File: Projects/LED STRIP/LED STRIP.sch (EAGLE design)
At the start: 70 parts, among them U1 PCA9635, U2 PCA9635, U3 PCA9635

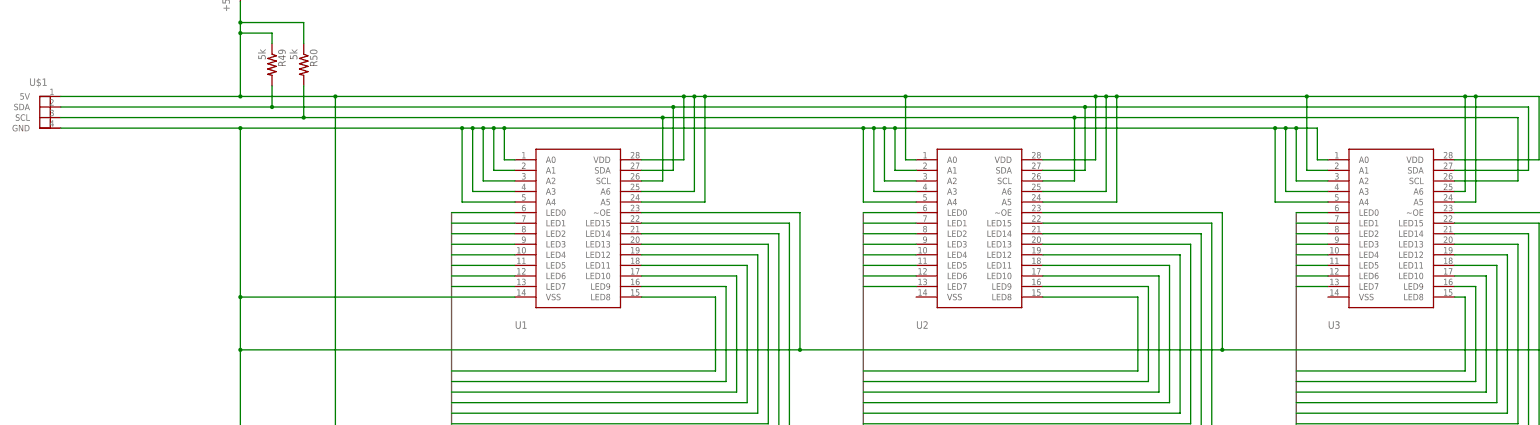
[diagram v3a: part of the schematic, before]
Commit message: design is done. ERC, DRC, air wires all pass. next up: integrate bluetooth components
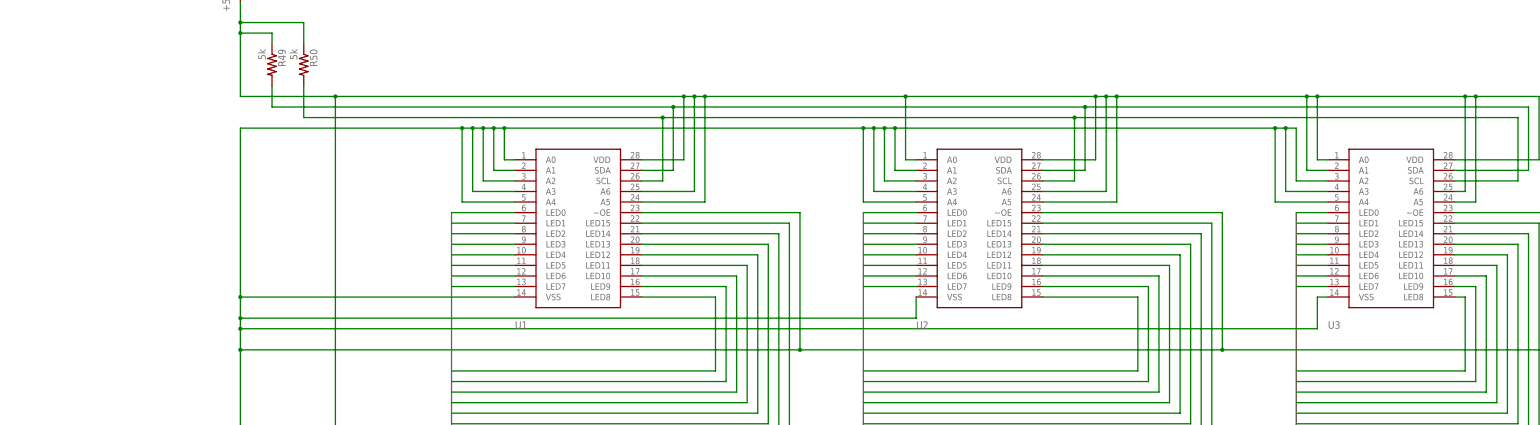
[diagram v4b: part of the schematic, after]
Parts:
- removed U$1: I2C_CONN, lightsuits:I2C_CONN
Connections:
- removed net N$51: R49.2, U$1.SDA, U1.SDA, U2.SDA, U3.SDA
- removed net N$52: R50.2, U$1.SCL, U1.SCL, U2.SCL, U3.SCL
- new net SCL: R50.2, U1.SCL, U2.SCL, U3.SCL
- new net SDA: R49.2, U1.SDA, U2.SDA, U3.SDA
- net +5V: now also U3.A0; no longer U$1.5V
- net GND: now also U2.VSS, U3.VSS; no longer U$1.GND, U3.A0
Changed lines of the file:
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@@
 <part name="P+1" library="supply1" deviceset="+5V" device=""/>
 <part name="GND1" library="supply1" deviceset="GND" device=""/>
-<part name="U$1" library="lightsuits" deviceset="I2C_CONN" device=""/>
 <part name="LED3" library="lightsuits" deviceset="LED_RGB" device=""/>
 <part name="LED4" library="lightsuits" deviceset="LED_RGB" device=""/>
@@
 <instance part="P+1" gate="1" x="-38.1" y="200.66"/>
 <instance part="GND1" gate="1" x="-38.1" y="5.08"/>
-<instance part="U$1" gate="G$1" x="-83.82" y="175.26"/>
 <instance part="LED3" gate="G$1" x="73.66" y="50.8"/>
 <instance part="LED4" gate="G$1" x="88.9" y="50.8"/>
@@
 <wire x1="-38.1" y1="7.62" x2="-38.1" y2="114.3" width="0.1524" layer="91"/>
 <pinref part="U1" gate="G$1" pin="VSS"/>
-<wire x1="-38.1" y1="114.3" x2="-38.1" y2="127" width="0.1524" layer="91"/>
+<wire x1="-38.1" y1="114.3" x2="-38.1" y2="119.38" width="0.1524" layer="91"/>
+<wire x1="-38.1" y1="119.38" x2="-38.1" y2="121.92" width="0.1524" layer="91"/>
+<wire x1="-38.1" y1="121.92" x2="-38.1" y2="127" width="0.1524" layer="91"/>
 <wire x1="-38.1" y1="127" x2="27.94" y2="127" width="0.1524" layer="91"/>
-<pinref part="U$1" gate="G$1" pin="GND"/>
-<wire x1="-81.28" y1="167.64" x2="-38.1" y2="167.64" width="0.1524" layer="91"/>
 <wire x1="-38.1" y1="167.64" x2="-38.1" y2="127" width="0.1524" layer="91"/>
 <junction x="-38.1" y="127"/>
@@
 <wire x1="116.84" y1="167.64" x2="119.38" y2="167.64" width="0.1524" layer="91"/>
 <wire x1="119.38" y1="167.64" x2="210.82" y2="167.64" width="0.1524" layer="91"/>
-<junction x="-38.1" y="167.64"/>
 <pinref part="U1" gate="G$1" pin="A0"/>
 <wire x1="210.82" y1="167.64" x2="213.36" y2="167.64" width="0.1524" layer="91"/>
 <wire x1="213.36" y1="167.64" x2="215.9" y2="167.64" width="0.1524" layer="91"/>
-<wire x1="215.9" y1="167.64" x2="220.98" y2="167.64" width="0.1524" layer="91"/>
 <wire x1="27.94" y1="160.02" x2="25.4" y2="160.02" width="0.1524" layer="91"/>
 <wire x1="25.4" y1="160.02" x2="25.4" y2="167.64" width="0.1524" layer="91"/>
@@
 <wire x1="119.38" y1="157.48" x2="119.38" y2="167.64" width="0.1524" layer="91"/>
 <junction x="119.38" y="167.64"/>
-<pinref part="U3" gate="G$1" pin="A0"/>
-<wire x1="223.52" y1="160.02" x2="220.98" y2="160.02" width="0.1524" layer="91"/>
-<wire x1="220.98" y1="160.02" x2="220.98" y2="167.64" width="0.1524" layer="91"/>
 <pinref part="U3" gate="G$1" pin="A2"/>
 <wire x1="223.52" y1="154.94" x2="215.9" y2="154.94" width="0.1524" layer="91"/>
 <wire x1="215.9" y1="154.94" x2="215.9" y2="167.64" width="0.1524" layer="91"/>
-<junction x="215.9" y="167.64"/>
 <pinref part="U2" gate="G$1" pin="A2"/>
 <wire x1="124.46" y1="154.94" x2="116.84" y2="154.94" width="0.1524" layer="91"/>
@@
 <wire x1="210.82" y1="149.86" x2="210.82" y2="167.64" width="0.1524" layer="91"/>
 <junction x="210.82" y="167.64"/>
+<pinref part="U2" gate="G$1" pin="VSS"/>
+<wire x1="124.46" y1="127" x2="124.46" y2="121.92" width="0.1524" layer="91"/>
+<wire x1="124.46" y1="121.92" x2="-38.1" y2="121.92" width="0.1524" layer="91"/>
+<junction x="-38.1" y="121.92"/>
+<pinref part="U3" gate="G$1" pin="VSS"/>
+<wire x1="223.52" y1="127" x2="220.98" y2="127" width="0.1524" layer="91"/>
+<wire x1="220.98" y1="127" x2="220.98" y2="119.38" width="0.1524" layer="91"/>
+<wire x1="220.98" y1="119.38" x2="-38.1" y2="119.38" width="0.1524" layer="91"/>
+<junction x="-38.1" y="119.38"/>
 </segment>
 </net>
@@
 <pinref part="P+1" gate="1" pin="+5V"/>
 <wire x1="-38.1" y1="198.12" x2="-38.1" y2="193.04" width="0.1524" layer="91"/>
-<pinref part="U$1" gate="G$1" pin="5V"/>
 <wire x1="-38.1" y1="193.04" x2="-38.1" y2="190.5" width="0.1524" layer="91"/>
 <wire x1="-38.1" y1="190.5" x2="-38.1" y2="175.26" width="0.1524" layer="91"/>
-<wire x1="-38.1" y1="175.26" x2="-81.28" y2="175.26" width="0.1524" layer="91"/>
 <wire x1="-38.1" y1="175.26" x2="-15.24" y2="175.26" width="0.1524" layer="91"/>
 <wire x1="-15.24" y1="175.26" x2="68.58" y2="175.26" width="0.1524" layer="91"/>
 <wire x1="68.58" y1="175.26" x2="68.58" y2="160.02" width="0.1524" layer="91"/>
-<junction x="-38.1" y="175.26"/>
 <pinref part="U1" gate="G$1" pin="VDD"/>
 <wire x1="68.58" y1="160.02" x2="58.42" y2="160.02" width="0.1524" layer="91"/>
@@
 <wire x1="170.18" y1="175.26" x2="172.72" y2="175.26" width="0.1524" layer="91"/>
 <wire x1="172.72" y1="175.26" x2="218.44" y2="175.26" width="0.1524" layer="91"/>
-<wire x1="218.44" y1="175.26" x2="256.54" y2="175.26" width="0.1524" layer="91"/>
+<wire x1="218.44" y1="175.26" x2="220.98" y2="175.26" width="0.1524" layer="91"/>
+<wire x1="220.98" y1="175.26" x2="256.54" y2="175.26" width="0.1524" layer="91"/>
 <wire x1="256.54" y1="175.26" x2="259.08" y2="175.26" width="0.1524" layer="91"/>
 <wire x1="259.08" y1="175.26" x2="274.32" y2="175.26" width="0.1524" layer="91"/>
@@
 <wire x1="-22.86" y1="193.04" x2="-38.1" y2="193.04" width="0.1524" layer="91"/>
 <junction x="-38.1" y="193.04"/>
+<pinref part="U3" gate="G$1" pin="A0"/>
+<wire x1="223.52" y1="160.02" x2="220.98" y2="160.02" width="0.1524" layer="91"/>
+<wire x1="220.98" y1="160.02" x2="220.98" y2="175.26" width="0.1524" layer="91"/>
+<junction x="220.98" y="175.26"/>
 </segment>
 </net>
@@
 </segment>
 </net>
-<net name="N$51" class="0">
-<segment>
-<pinref part="U$1" gate="G$1" pin="SDA"/>
+<net name="SDA" class="0">
+<segment>
 <pinref part="U1" gate="G$1" pin="SDA"/>
 <wire x1="58.42" y1="157.48" x2="66.04" y2="157.48" width="0.1524" layer="91"/>
@@
 <pinref part="U3" gate="G$1" pin="SDA"/>
 <wire x1="271.78" y1="157.48" x2="254" y2="157.48" width="0.1524" layer="91"/>
-<wire x1="-81.28" y1="172.72" x2="-30.48" y2="172.72" width="0.1524" layer="91"/>
 <junction x="66.04" y="172.72"/>
 <pinref part="R49" gate="G$1" pin="2"/>
 <wire x1="-30.48" y1="172.72" x2="66.04" y2="172.72" width="0.1524" layer="91"/>
 <wire x1="-30.48" y1="177.8" x2="-30.48" y2="172.72" width="0.1524" layer="91"/>
-<junction x="-30.48" y="172.72"/>
-</segment>
-</net>
-<net name="N$52" class="0">
-<segment>
-<pinref part="U$1" gate="G$1" pin="SCL"/>
+</segment>
+</net>
+<net name="SCL" class="0">
+<segment>
 <wire x1="63.5" y1="170.18" x2="63.5" y2="154.94" width="0.1524" layer="91"/>
 <pinref part="U1" gate="G$1" pin="SCL"/>
@@
 <pinref part="U3" gate="G$1" pin="SCL"/>
 <wire x1="269.24" y1="154.94" x2="254" y2="154.94" width="0.1524" layer="91"/>
-<wire x1="-81.28" y1="170.18" x2="-22.86" y2="170.18" width="0.1524" layer="91"/>
 <junction x="63.5" y="170.18"/>
 <pinref part="R50" gate="G$1" pin="2"/>
 <wire x1="-22.86" y1="170.18" x2="63.5" y2="170.18" width="0.1524" layer="91"/>
 <wire x1="-22.86" y1="177.8" x2="-22.86" y2="170.18" width="0.1524" layer="91"/>
-<junction x="-22.86" y="170.18"/>
-</segment>
-</net>
+</segment>
+</net>
